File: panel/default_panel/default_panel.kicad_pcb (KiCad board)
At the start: 2 copper layers, 100 x 100 mm, 1 part

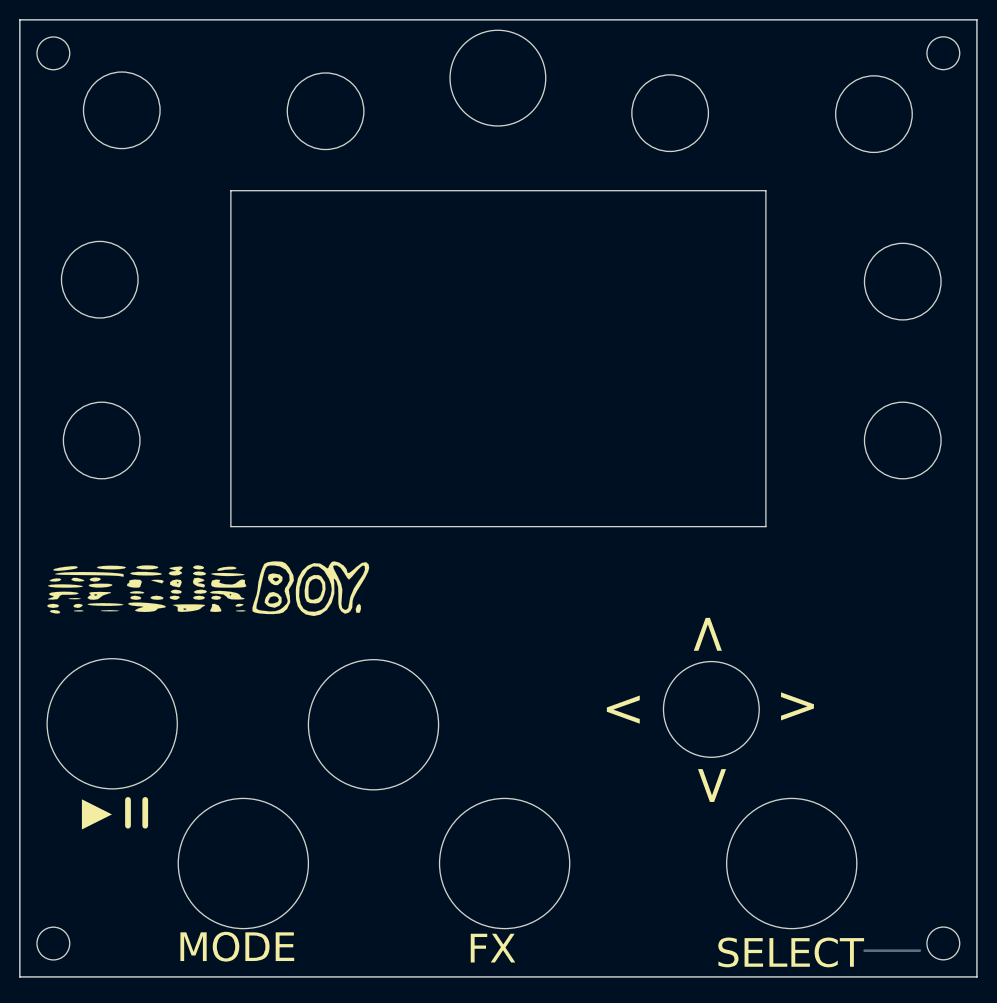
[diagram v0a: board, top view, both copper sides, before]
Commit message: update panel with changes based on last one
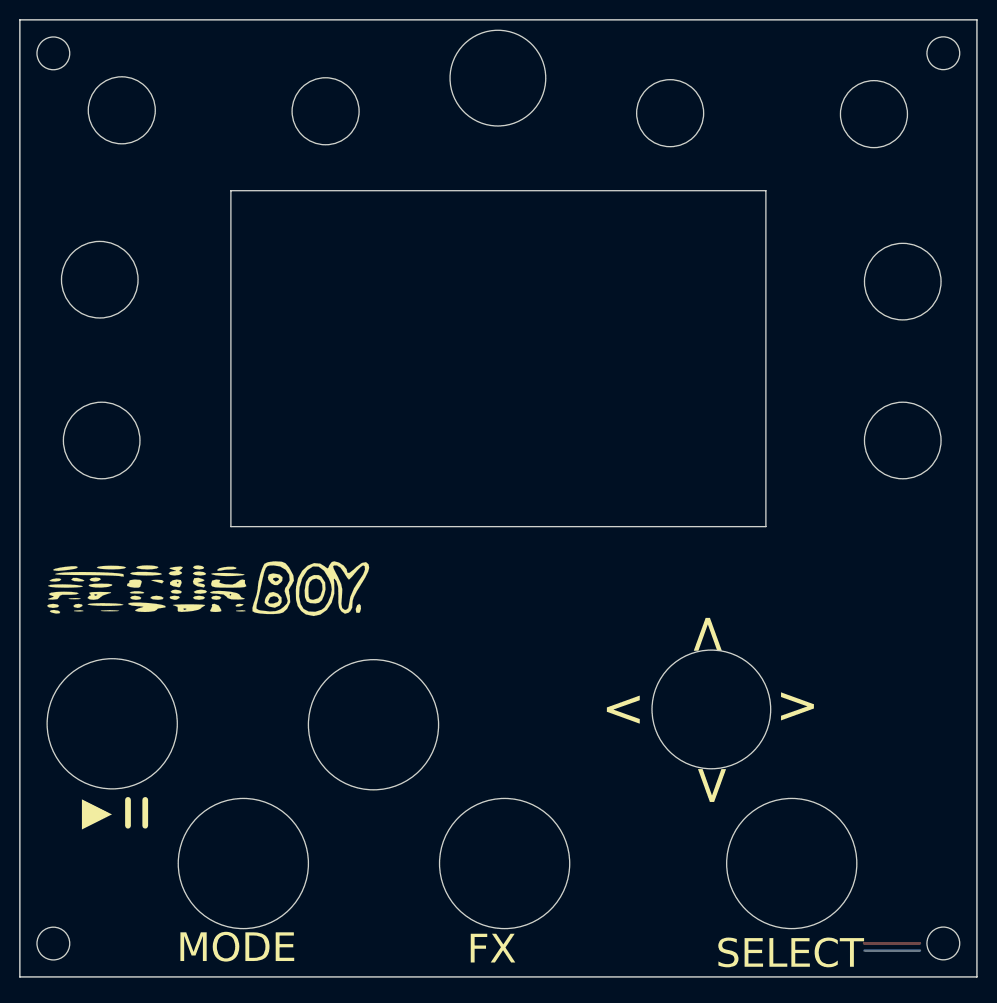
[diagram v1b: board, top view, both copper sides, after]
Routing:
- net (no net): track 5.80 -> 11.6 mm
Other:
- outline, holes or cut-outs redrawn
- board text added: "cyberboy666 & ichi raramuri recurBOY panel for v0_7_1 mk_ii"
- board text removed: "cyberboy666 & ichi raramuri recurBOY panel v0_7_1"
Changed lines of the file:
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@@
   (gr_circle (center 178.138276 48.238276) (end 179.838276 48.038276) (layer "Edge.Cuts") (width 0.1) (fill none))
   (gr_circle (center 90.2 88.7) (end 94.2 88.7) (layer "Edge.Cuts") (width 0.1) (fill none))
-  (gr_circle (center 92.3 54.2) (end 96.3 54.2) (layer "Edge.Cuts") (width 0.1) (fill none))
-  (gr_circle (center 170.889752 54.6) (end 174.889752 54.6) (layer "Edge.Cuts") (width 0.1) (fill none))
+  (gr_circle (center 92.3 54.2) (end 95.8 54.2) (layer "Edge.Cuts") (width 0.1) (fill none))
+  (gr_circle (center 170.889752 54.6) (end 174.389752 54.6) (layer "Edge.Cuts") (width 0.1) (fill none))
   (gr_circle (center 90 71.9) (end 94 71.9) (layer "Edge.Cuts") (width 0.1) (fill none))
-  (gr_circle (center 113.594876 54.3) (end 117.594876 54.3) (layer "Edge.Cuts") (width 0.1) (fill none))
+  (gr_circle (center 113.594876 54.3) (end 117.094876 54.3) (layer "Edge.Cuts") (width 0.1) (fill none))
   (gr_circle (center 85.15 141.261724) (end 86.85 141.061724) (layer "Edge.Cuts") (width 0.1) (fill none))
-  (gr_circle (center 149.594876 54.5) (end 153.594876 54.5) (layer "Edge.Cuts") (width 0.1) (fill none))
+  (gr_circle (center 149.594876 54.5) (end 153.094876 54.5) (layer "Edge.Cuts") (width 0.1) (fill none))
   (gr_line (start 81.65 44.75) (end 181.65 44.75) (layer "Edge.Cuts") (width 0.15))
   (gr_rect (start 103.7 62.6) (end 159.6 97.7) (layer "Edge.Cuts") (width 0.1) (fill none))
-  (gr_circle (center 153.9 116.8) (end 158.9 116.8) (layer "Edge.Cuts") (width 0.1) (fill none))
+  (gr_circle (center 153.9 116.8) (end 160.1 116.8) (layer "Edge.Cuts") (width 0.1) (fill none))
   (gr_circle (center 173.9 88.7) (end 177.9 88.7) (layer "Edge.Cuts") (width 0.1) (fill none))
   (gr_circle (center 132.3 132.9) (end 139.1 132.9) (layer "Edge.Cuts") (width 0.1) (fill none))
@@
     (effects (font (size 5 5) (thickness 0.5)) (justify mirror))
   )
-  (gr_text "cyberboy666 & ichi raramuri\nrecurBOY panel v0_7_1" (at 179 131.7 270) (layer "B.SilkS")
+  (gr_text "cyberboy666 & ichi raramuri\nrecurBOY panel for v0_7_1 mk_ii" (at 179 131.7 270) (layer "B.SilkS")
     (effects (font (size 1.2 1.2) (thickness 0.3)) (justify left mirror))
   )
@@
     (effects (font (size 4 4) (thickness 0.8)))
   )
+  (segment (start 169.85 141.25) (end 175.7 141.25) (width 0.25) (layer "F.Cu") (net 0))
   (segment (start 175.7 142) (end 169.9 142) (width 0.25) (layer "B.Cu") (net 0))
 )
